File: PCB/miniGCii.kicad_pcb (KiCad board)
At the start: 2 copper layers, 35 x 19 mm, 5 parts, among them J1 AudioJack4, J2 AudioJack4, J3 Conn_01x05_Pin

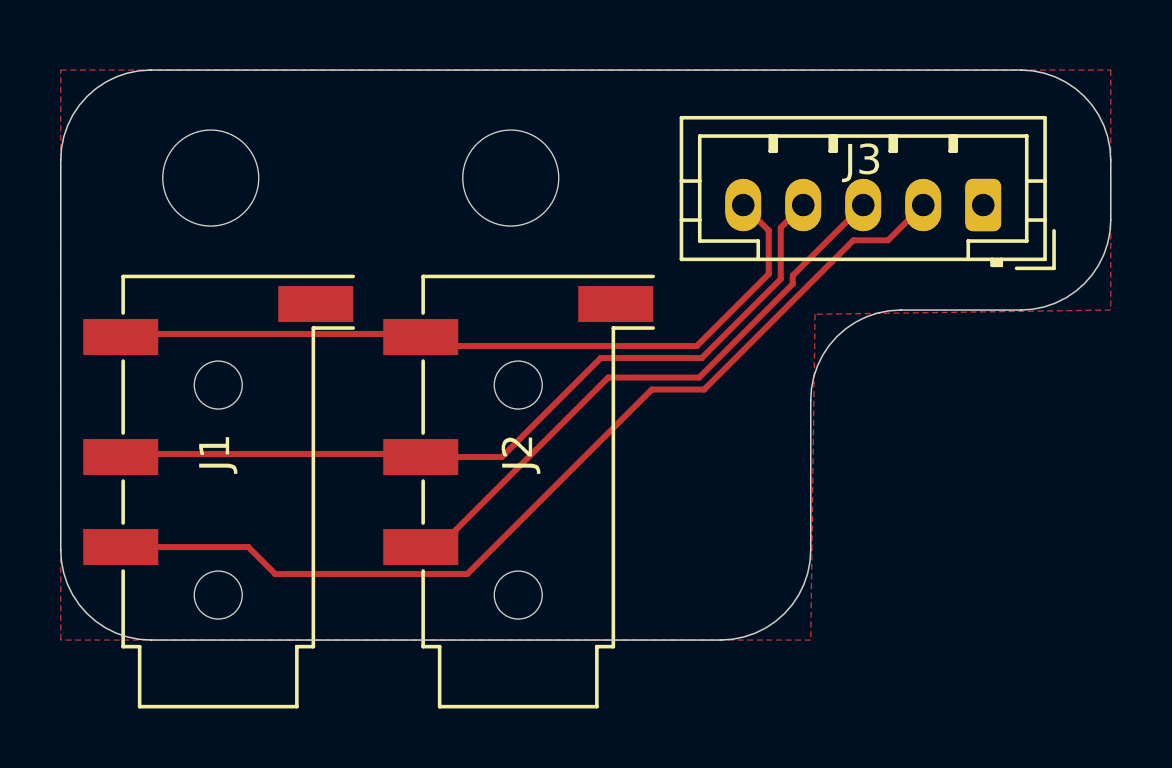
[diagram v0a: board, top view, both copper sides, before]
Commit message: Added silkscreen, resized PCB
Signed-off-by: Devnol <pgkoutsoumanis@gmail.com>
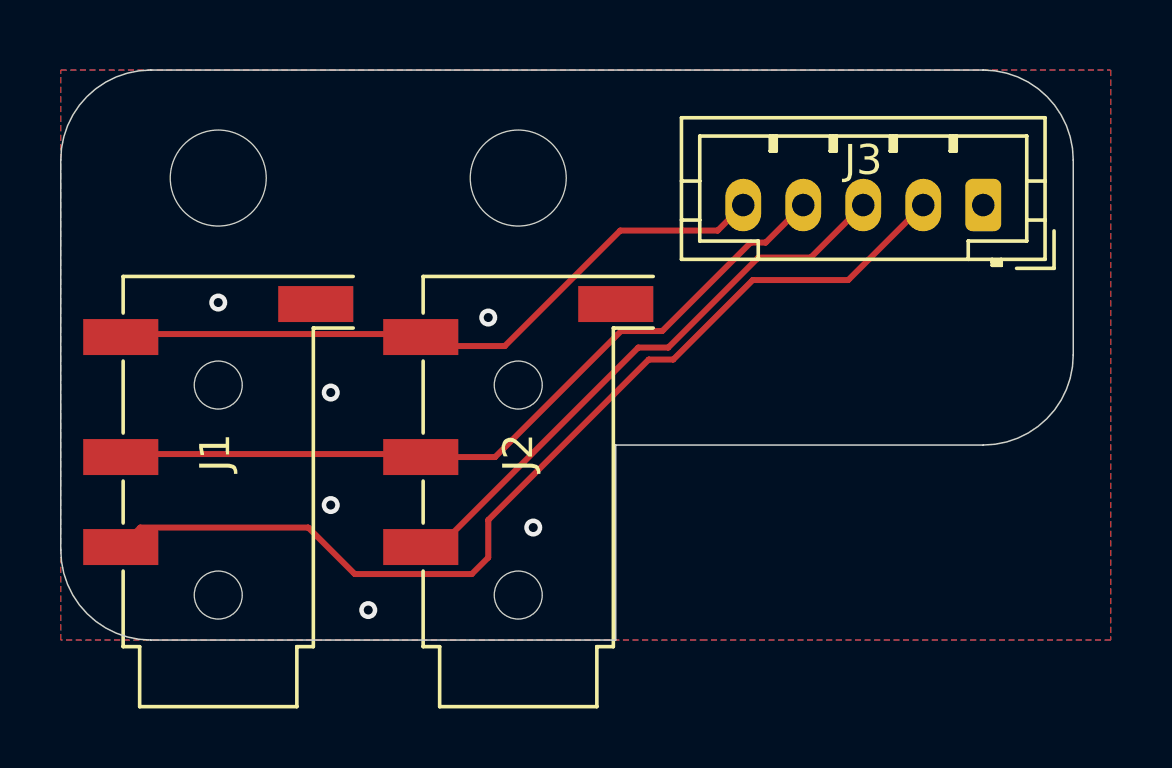
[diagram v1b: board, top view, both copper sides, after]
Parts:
- moved REF** 0.25 mm to (143.2, 105.6)
- moved REF** 0.25 mm to (133.2, 105.6)
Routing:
- net /5V: track 25.6 -> 23.1 mm
- net /DAT1: track 32.2 -> 33.5 mm
- net /3v3: track 27.5 -> 26.5 mm
- net /GND: vias 0 -> 6
- added copper zone on B.Cu, net /GND
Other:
- board size 35 x 19 mm -> 33.8 x 19 mm
- board text added: "github.com/Wii-mini-Hacking/miniGCii"
- board text added: "miniGCii Breakout rev1.0 Designed in Greece with by Devnol"
- board text added: "♥︎"

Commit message: Added pad silks, exported PCB STEP
Signed-off-by: Devnol <pgkoutsoumanis@gmail.com>
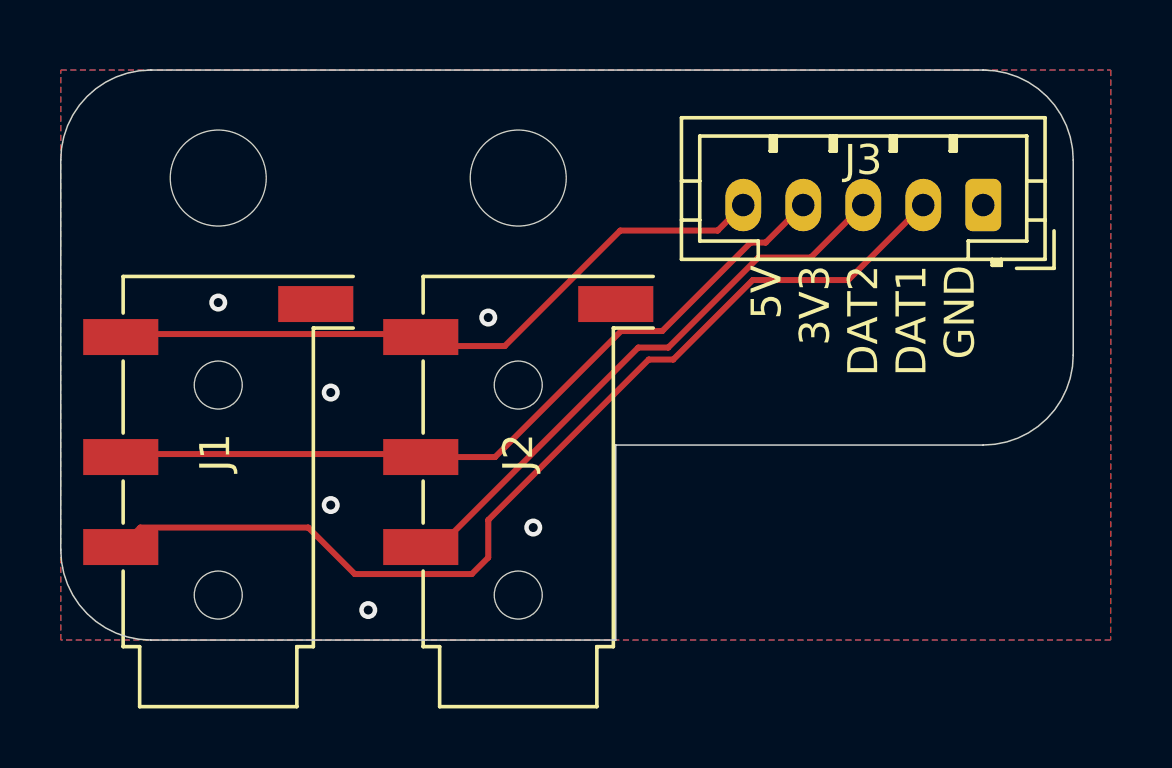
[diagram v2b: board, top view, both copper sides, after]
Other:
- board text added: "5V 3V3 DAT2 DAT1 GND"
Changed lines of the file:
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@@
+		)
+	)
+	(gr_text "5V\n3V3\nDAT2\nDAT1\nGND"
+		(at 154.75 108.5 90)
+		(layer "F.SilkS")
+		(effects
+			(font
+				(size 1 1)
+				(thickness 0.1)
+			)
+			(justify right)
 		)
 	)

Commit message: changed connector to 90deg, added fabrication outputs
Signed-off-by: Devnol <pgkoutsoumanis@gmail.com>
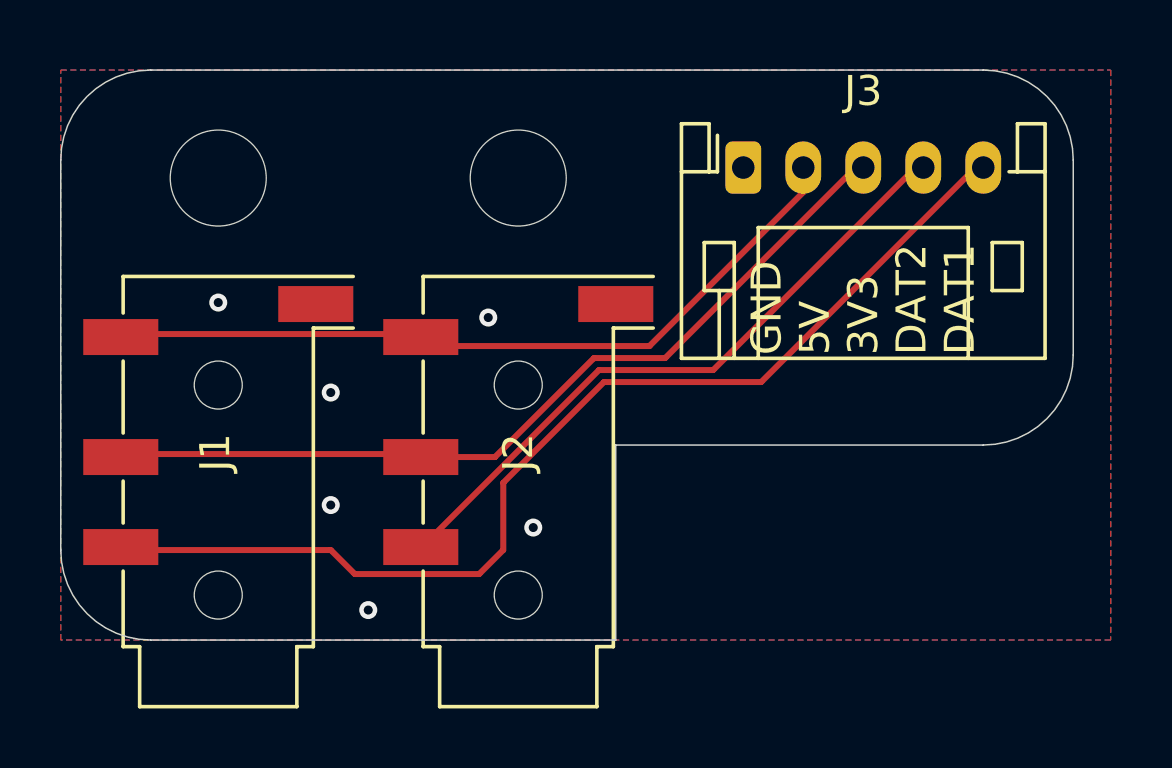
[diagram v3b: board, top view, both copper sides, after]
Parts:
- J3: footprint Connector_JST:JST_PH_B5B-PH-K_1x05_P2.00mm_Vertical -> Connector_JST:JST_PH_S5B-PH-K_1x05_P2.00mm_Horizontal
- moved J3 8.10 mm to (150.8, 105.2), turned to 0 degrees
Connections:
- J3 pad 2: /DAT1 -> /5V
- J3 pad 3: /DAT2 -> /3v3
- J3 pad 4: /3v3 -> /DAT2
- J3 pad 5: /5V -> /DAT1
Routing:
- net /5V: track 23.1 -> 26.3 mm
- net /DAT1: track 33.5 -> 36.2 mm
- net /3v3: track 26.5 -> 29.1 mm
- net /DAT2: track 19.5 -> 22.1 mm
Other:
- board text added: "GND 5V 3V3 DAT2 DAT1"
- board text removed: "5V 3V3 DAT2 DAT1 GND"
